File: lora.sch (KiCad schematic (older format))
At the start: 62 parts, among them J1 Conn_01x02, J11 Conn_Coaxial, J2 Humidity, J3 Temp, J4 Programming_Jumper, J5 Temp, J6 VDD, J7 GPS, J8 SIM800, J9 I2C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

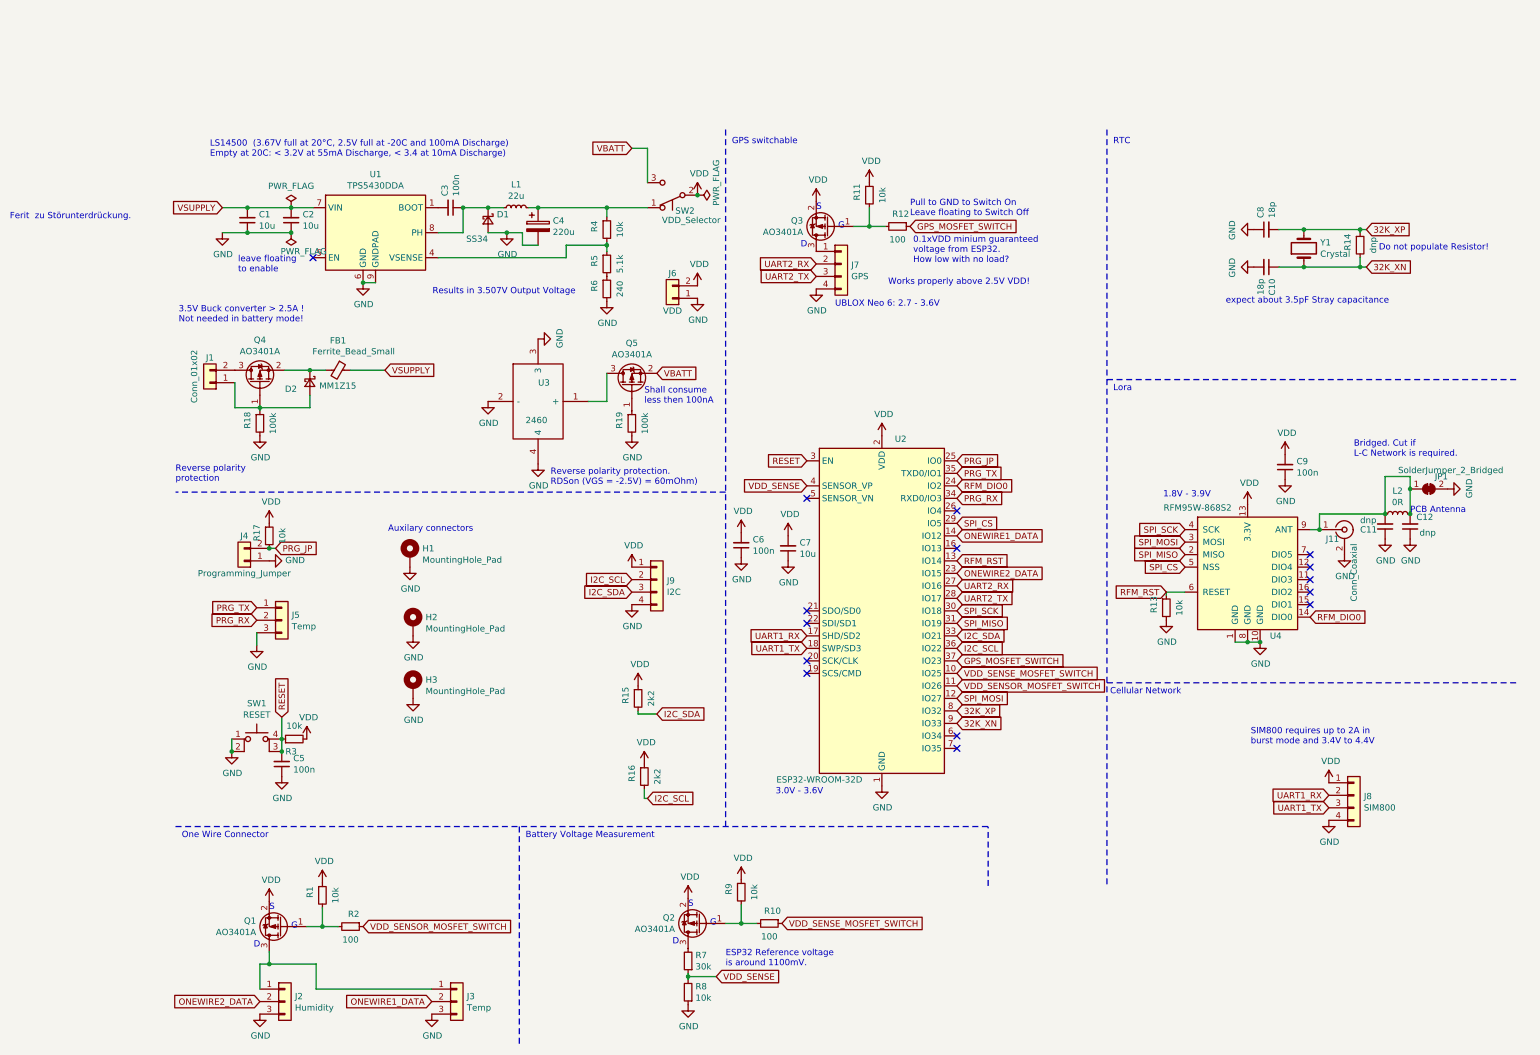
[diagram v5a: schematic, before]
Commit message: - updated pin assignment to recommended pins. - added 100uF capacity to buffer spike loads in battery mode.
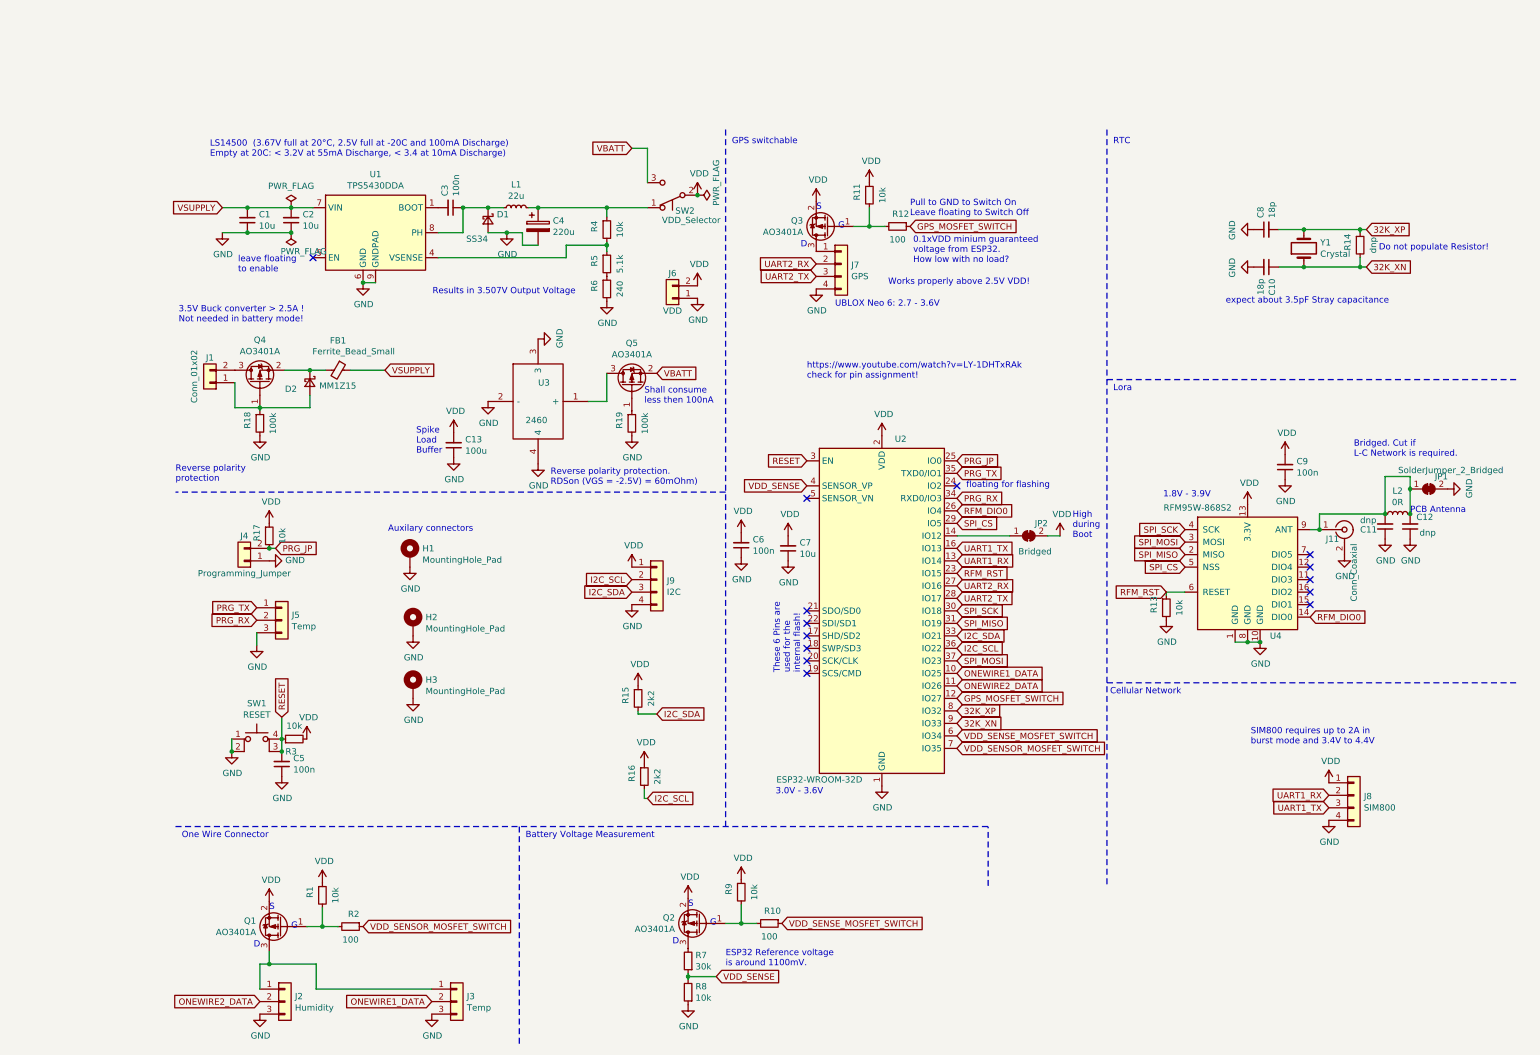
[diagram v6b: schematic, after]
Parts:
- added C13: 100u, Capacitor_SMD:C_1206_3216Metric, symbol Device:C_Small
- added JP2: Bridged, Jumper:SolderJumper-2_P1.3mm_Bridged_Pad1.0x1.5mm, symbol Jumper:SolderJumper_2_Bridged
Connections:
- net GND: now also C13.1
- net GPS_MOSFET_SWITCH: now also U2.12 (IO27); no longer U2.37 (IO23)
- net ONEWIRE1_DATA: now also U2.10 (IO25); no longer U2.14 (IO12)
- net ONEWIRE2_DATA: now also U2.11 (IO26); no longer U2.23 (IO15)
- net RFM_DIO0: now also U2.26 (IO4); no longer U2.24 (IO2)
- net RFM_RST: now also U2.23 (IO15); no longer U2.13 (IO14)
- net SPI_MOSI: now also U2.37 (IO23); no longer U2.12 (IO27)
- net UART1_RX: now also U2.13 (IO14); no longer U2.17 (SHD/SD2)
- net UART1_TX: now also U2.16 (IO13); no longer U2.18 (SWP/SD3)
- net VDD: now also C13.2, JP2.2 (B)
- net VDD_SENSE_MOSFET_SWITCH: now also U2.6 (IO34); no longer U2.10 (IO25)
- net VDD_SENSOR_MOSFET_SWITCH: now also U2.7 (IO35); no longer U2.11 (IO26)
- new net: JP2.1 (A), U2.14 (IO12)
- no-connect marks 15 -> 14
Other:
- note added: "High \nduring \nBoot"
- note added: "Spike \nLoad\nBuffer"
- note added: "These 6 Pins are\nused for the\ninternal flash!"
- note added: "floating for flashing"
- note added: "https://www.youtube.com/watch?v=LY-1DHTxRAk\ncheck for pin assignment!"
- note removed: "Ferit zu Störunterdrückung."
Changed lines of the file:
@@
 	-1   0    0    1
 $EndComp
-Text GLabel 6725 4925 2    50   Input ~ 0
+Text GLabel 6725 5425 2    50   Input ~ 0
 VDD_SENSOR_MOSFET_SWITCH
 $Comp
@@
 	-1   0    0    1
 $EndComp
-Text GLabel 6725 4825 2    50   Input ~ 0
+Text GLabel 6725 5325 2    50   Input ~ 0
 VDD_SENSE_MOSFET_SWITCH
 Text GLabel 5525 3325 0    50   Input ~ 0
 VDD_SENSE
-Text GLabel 5525 4625 0    50   Input ~ 0
+Text GLabel 6725 3825 2    50   Input ~ 0
 UART1_TX
-Text GLabel 5525 4525 0    50   Input ~ 0
+Text GLabel 6725 3925 2    50   Input ~ 0
 UART1_RX
-Text GLabel 6725 3725 2    50   Input ~ 0
+Text GLabel 6725 4825 2    50   Input ~ 0
 ONEWIRE1_DATA
 Text GLabel 6725 4225 2    50   Input ~ 0
@@
 Text GLabel 5525 3125 0    50   Input ~ 0
 RESET
-Text GLabel 6725 3325 2    50   Input ~ 0
+Text GLabel 6725 3525 2    50   Input ~ 0
 RFM_DIO0
+Text GLabel 6725 4925 2    50   Input ~ 0
+ONEWIRE2_DATA
 Text GLabel 6725 4025 2    50   Input ~ 0
-ONEWIRE2_DATA
-Text GLabel 6725 3925 2    50   Input ~ 0
 RFM_RST
-Text GLabel 6725 5025 2    50   Input ~ 0
+Text GLabel 6725 4725 2    50   Input ~ 0
 SPI_MOSI
 Text GLabel 6725 4425 2    50   Input ~ 0
@@
 Text GLabel 6725 4625 2    50   Input ~ 0
 I2C_SCL
-Text GLabel 6725 4725 2    50   Input ~ 0
+Text GLabel 6725 5025 2    50   Input ~ 0
 GPS_MOSFET_SWITCH
 Text GLabel 6725 3125 2    50   Input ~ 0
@@
 L power:GND #PWR0147
 U 1 1 5FBDD884
-P 4125 2925
-F 0 "#PWR0147" H 4125 2675 50  0001 C CNN
-F 1 "GND" H 4130 2752 50  0000 C CNN
-F 2 "" H 4125 2925 50  0001 C CNN
-F 3 "" H 4125 2925 50  0001 C CNN
-	1    4125 2925
+P 2700 3100
+F 0 "#PWR0147" H 2700 2850 50  0001 C CNN
+F 1 "GND" H 2705 2927 50  0000 C CNN
+F 2 "" H 2700 3100 50  0001 C CNN
+F 3 "" H 2700 3100 50  0001 C CNN
+	1    2700 3100
 	1    0    0    -1
 $EndComp
@@
 	-1   0    0    1
 $EndComp
-Text Notes -850 1200 0    50   ~ 0
-Ferit  zu Störunterdrückung.
 Text Notes 2175 3700 0    50   ~ 0
 Auxilary connectors
-NoConn ~ 6725 3525
-NoConn ~ 6725 3825
-NoConn ~ 6725 5325
-NoConn ~ 6725 5425
 NoConn ~ 5525 3425
 $Comp
@@
 	1    0    0    -1
 $EndComp
+$Comp
+L Device:C_Small C13
+U 1 1 5FBD5D0C
+P 2700 3000
+F 0 "C13" H 2608 2954 50  0000 R CNN
+F 1 "100u" H 2608 3045 50  0000 R CNN
+F 2 "Capacitor_SMD:C_1206_3216Metric" H 2700 3000 50  0001 C CNN
+F 3 "~" H 2700 3000 50  0001 C CNN
+F 4 "C15008" H 2700 3000 50  0001 C CNN "LCSC"
+	1    2700 3000
+	-1   0    0    1
+$EndComp
+Text Notes 5525 2475 0    50   ~ 0
+https://www.youtube.com/watch?v=LY-1DHTxRAk\ncheck for pin assignment!
+NoConn ~ 6725 3325
+Text Notes 7650 3750 0    50   ~ 0
+High \nduring \nBoot
+Text Notes 5475 4825 1    50   ~ 0
+These 6 Pins are\nused for the\ninternal flash!
+NoConn ~ 5525 4525
+NoConn ~ 5525 4625
+$Comp
+L power:VDD #PWR06
+U 1 1 5FD0859A
+P 7550 3725
+F 0 "#PWR06" H 7550 3575 50  0001 C CNN
+F 1 "VDD" H 7565 3898 50  0000 C CNN
+F 2 "" H 7550 3725 50  0001 C CNN
+F 3 "" H 7550 3725 50  0001 C CNN
+	1    7550 3725
+	1    0    0    -1
+$EndComp
+$Comp
+L Jumper:SolderJumper_2_Bridged JP2
+U 1 1 5FD08A69
+P 7300 3725
+F 0 "JP2" H 7400 3825 50  0000 C CNN
+F 1 "Bridged" H 7350 3600 50  0000 C CNN
+F 2 "Jumper:SolderJumper-2_P1.3mm_Bridged_Pad1.0x1.5mm" H 7300 3725 50  0001 C CNN
+F 3 "~" H 7300 3725 50  0001 C CNN
+	1    7300 3725
+	1    0    0    -1
+$EndComp
+Wire Wire Line
+	7150 3725 6725 3725
+Wire Wire Line
+	7550 3725 7450 3725
+Text Notes 6800 3350 0    50   ~ 0
+floating for flashing
+$Comp
+L power:VDD #PWR0150
+U 1 1 5FD14806
+P 2700 2900
+F 0 "#PWR0150" H 2700 2750 50  0001 C CNN
+F 1 "VDD" H 2715 3073 50  0000 C CNN
+F 2 "" H 2700 2900 50  0001 C CNN
+F 3 "" H 2700 2900 50  0001 C CNN
+	1    2700 2900
+	1    0    0    -1
+$EndComp
+Text Notes 2400 3075 0    50   ~ 0
+Spike \nLoad\nBuffer
+$Comp
+L power:GND #PWR0151
+U 1 1 5FD1B773
+P 4125 2925
+F 0 "#PWR0151" H 4125 2675 50  0001 C CNN
+F 1 "GND" H 4130 2752 50  0000 C CNN
+F 2 "" H 4125 2925 50  0001 C CNN
+F 3 "" H 4125 2925 50  0001 C CNN
+	1    4125 2925
+	1    0    0    -1
+$EndComp

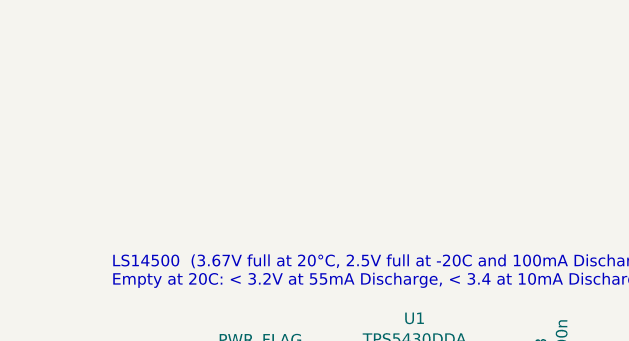
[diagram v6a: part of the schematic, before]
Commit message: added page legend.
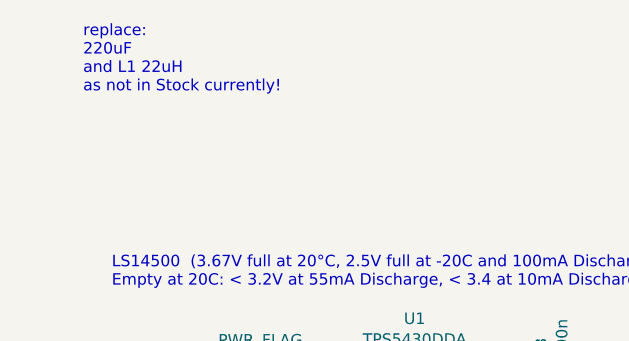
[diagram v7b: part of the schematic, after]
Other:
- note added: "replace:\n220uF \nand L1 22uH \nas not in Stock currently!"
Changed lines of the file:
@@
 encoding utf-8
 Sheet 1 1
-Title ""
-Date ""
-Rev ""
+Title "Lora Vision (as Sensor or Gateway)"
+Date "2020-12-08"
+Rev "v1.0"
 Comp ""
 Comment1 ""
@@
 	1    0    0    -1
 $EndComp
+Text Notes 625  -150 0    50   ~ 0
+replace:\n220uF \nand L1 22uH    \nas not in Stock currently!
 $EndSCHEMATC

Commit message: intermediate commit before removing a mounting hole
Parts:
- J1: footprint Connector_PinHeader_2.54mm:PinHeader_1x02_P2.54mm_Vertical -> Connector_PinHeader_2.54mm:PinHeader_1x02_P2.54mm_Horizontal
- J2, J3: footprint Connector_PinHeader_2.54mm:PinHeader_1x03_P2.54mm_Vertical -> Connector_PinHeader_2.54mm:PinHeader_1x03_P2.54mm_Horizontal
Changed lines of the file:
@@
 F 0 "J2" H 1430 7492 50  0000 L CNN
 F 1 "Humidity" H 1430 7401 50  0000 L CNN
-F 2 "Connector_PinHeader_2.54mm:PinHeader_1x03_P2.54mm_Vertical" H 1350 7450 50  0001 C CNN
+F 2 "Connector_PinHeader_2.54mm:PinHeader_1x03_P2.54mm_Horizontal" H 1350 7450 50  0001 C CNN
 F 3 "~" H 1350 7450 50  0001 C CNN
 	1    1350 7450
@@
 F 0 "J1" H 750 2300 50  0000 C CNN
 F 1 "Conn_01x02" V 875 2450 50  0000 C CNN
-F 2 "Connector_PinHeader_2.54mm:PinHeader_1x02_P2.54mm_Vertical" H 750 2500 50  0001 C CNN
+F 2 "Connector_PinHeader_2.54mm:PinHeader_1x02_P2.54mm_Horizontal" H 750 2500 50  0001 C CNN
 F 3 "~" H 750 2500 50  0001 C CNN
 	1    750  2500
@@
 F 0 "J3" H 2805 7492 50  0000 L CNN
 F 1 "Temp" H 2805 7401 50  0000 L CNN
-F 2 "Connector_PinHeader_2.54mm:PinHeader_1x03_P2.54mm_Vertical" H 2725 7450 50  0001 C CNN
+F 2 "Connector_PinHeader_2.54mm:PinHeader_1x03_P2.54mm_Horizontal" H 2725 7450 50  0001 C CNN
 F 3 "~" H 2725 7450 50  0001 C CNN
 	1    2725 7450
